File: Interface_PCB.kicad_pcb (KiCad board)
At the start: 2 copper layers, 46.5 x 47.9 mm, 46 parts, among them IC1 STM32L412RBT6P, U1 AMS1117-3.3, Y1 Crystal, Y2 Crystal

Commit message: Added BOM, position and gerber files
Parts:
- LMS1: footprint Capacitor_SMD:C_0603_1608Metric -> Inductor_SMD:L_0603_1608Metric
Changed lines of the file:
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@@
       (drillshape 0)
       (scaleselection 1)
-      (outputdirectory "drill files/")
+      (outputdirectory "drill files/gerber/")
     )
   )
@@
     )
     (fp_line (start -4.65 -4.65) (end 4.65 -4.65) (layer "F.SilkS") (width 0.2))
-    (fp_line (start -4.65 4.65) (end -4.65 -4.65) (layer "F.SilkS") (width 0.2))
     (fp_line (start 4.65 4.65) (end -4.65 4.65) (layer "F.SilkS") (width 0.2))
+    (fp_line (start -4.65 4.65) (end -4.65 -4.65) (layer "F.SilkS") (width 0.2))
     (fp_line (start 4.65 -4.65) (end 4.65 4.65) (layer "F.SilkS") (width 0.2))
     (fp_circle (center -6.225 -4.5) (end -6.225 -4.375) (layer "F.SilkS") (width 0.25) (fill none))
-    (fp_line (start -6.725 -6.725) (end 6.725 -6.725) (layer "F.CrtYd") (width 0.05))
     (fp_line (start 6.725 -6.725) (end 6.725 6.725) (layer "F.CrtYd") (width 0.05))
-    (fp_line (start -6.725 6.725) (end -6.725 -6.725) (layer "F.CrtYd") (width 0.05))
     (fp_line (start 6.725 6.725) (end -6.725 6.725) (layer "F.CrtYd") (width 0.05))
+    (fp_line (start -6.725 -6.725) (end 6.725 -6.725) (layer "F.CrtYd") (width 0.05))
+    (fp_line (start -6.725 6.725) (end -6.725 -6.725) (layer "F.CrtYd") (width 0.05))
+    (fp_line (start -5 -4.5) (end -4.5 -5) (layer "F.Fab") (width 0.1))
+    (fp_line (start 5 -5) (end 5 5) (layer "F.Fab") (width 0.1))
     (fp_line (start -5 5) (end -5 -5) (layer "F.Fab") (width 0.1))
     (fp_line (start -5 -5) (end 5 -5) (layer "F.Fab") (width 0.1))
     (fp_line (start 5 5) (end -5 5) (layer "F.Fab") (width 0.1))
-    (fp_line (start 5 -5) (end 5 5) (layer "F.Fab") (width 0.1))
-    (fp_line (start -5 -4.5) (end -4.5 -5) (layer "F.Fab") (width 0.1))
     (pad "1" smd rect locked (at -5.738 -3.75 90) (size 0.3 1.475) (layers "F.Cu" "F.Paste" "F.Mask")
       (net 3 "+3V3") (pinfunction "VBAT") (pintype "passive"))
@@
     (pad "" np_thru_hole circle (at 0 0) (size 2.1 2.1) (drill 2.1) (layers *.Cu *.Mask))
   )
-  (footprint "Capacitor_SMD:C_0603_1608Metric" (layer "F.Cu")
+  (footprint "Inductor_SMD:L_0603_1608Metric" (layer "F.Cu")
     (at 127.0508 111.506)
-    (descr "Capacitor SMD 0603 (1608 Metric), square (rectangular) end terminal, IPC_7351 nominal, (Body size source: IPC-SM-782 page 76, https://www.pcb-3d.com/wordpress/wp-content/uploads/ipc-sm-782a_amendment_1_and_2.pdf), generated with kicad-footprint-generator")
-    (tags "capacitor")
+    (descr "Inductor SMD 0603 (1608 Metric), square (rectangular) end terminal, IPC_7351 nominal, (Body size source: http://www.tortai-tech.com/upload/download/2011102023233369053.pdf), generated with kicad-footprint-generator")
+    (tags "inductor")
     (property "Sheetfile" "Interface_PCB.kicad_sch")
     (property "Sheetname" "")
     (attr smd)
-    (fp_text reference "LMS1" (at -2.54 -0.0254 180) (layer "F.SilkS")
-      (effects (font (size 0.5 0.5) (thickness 0.125)))
+    (fp_text reference "LMS1" (at -3.302 0.0254) (layer "F.SilkS")
+      (effects (font (size 1 1) (thickness 0.15)))
     )
     (fp_text value "39nH" (at 0 1.43) (layer "F.Fab")
@@
       (effects (font (size 0.4 0.4) (thickness 0.06)))
     )
-    (fp_line (start -0.14058 -0.51) (end 0.14058 -0.51) (layer "F.SilkS") (width 0.12))
-    (fp_line (start -0.14058 0.51) (end 0.14058 0.51) (layer "F.SilkS") (width 0.12))
+    (fp_line (start -0.162779 -0.51) (end 0.162779 -0.51) (layer "F.SilkS") (width 0.12))
+    (fp_line (start -0.162779 0.51) (end 0.162779 0.51) (layer "F.SilkS") (width 0.12))
     (fp_line (start -1.48 -0.73) (end 1.48 -0.73) (layer "F.CrtYd") (width 0.05))
-    (fp_line (start 1.48 -0.73) (end 1.48 0.73) (layer "F.CrtYd") (width 0.05))
     (fp_line (start -1.48 0.73) (end -1.48 -0.73) (layer "F.CrtYd") (width 0.05))
+    (fp_line (start 1.48 -0.73) (end 1.48 0.73) (layer "F.CrtYd") (width 0.05))
     (fp_line (start 1.48 0.73) (end -1.48 0.73) (layer "F.CrtYd") (width 0.05))
-    (fp_line (start -0.8 0.4) (end -0.8 -0.4) (layer "F.Fab") (width 0.1))
+    (fp_line (start 0.8 -0.4) (end 0.8 0.4) (layer "F.Fab") (width 0.1))
     (fp_line (start -0.8 -0.4) (end 0.8 -0.4) (layer "F.Fab") (width 0.1))
+    (fp_line (start -0.8 0.4) (end -0.8 -0.4) (layer "F.Fab") (width 0.1))
     (fp_line (start 0.8 0.4) (end -0.8 0.4) (layer "F.Fab") (width 0.1))
-    (fp_line (start 0.8 -0.4) (end 0.8 0.4) (layer "F.Fab") (width 0.1))
-    (pad "1" smd roundrect (at -0.775 0) (size 0.9 0.95) (layers "F.Cu" "F.Paste" "F.Mask") (roundrect_rratio 0.25)
+    (pad "1" smd roundrect (at -0.7875 0) (size 0.875 0.95) (layers "F.Cu" "F.Paste" "F.Mask") (roundrect_rratio 0.25)
       (net 3 "+3V3") (pinfunction "1") (pintype "passive"))
-    (pad "2" smd roundrect (at 0.775 0) (size 0.9 0.95) (layers "F.Cu" "F.Paste" "F.Mask") (roundrect_rratio 0.25)
+    (pad "2" smd roundrect (at 0.7875 0) (size 0.875 0.95) (layers "F.Cu" "F.Paste" "F.Mask") (roundrect_rratio 0.25)
       (net 4 "+3.3VA") (pinfunction "2") (pintype "passive"))
-    (model "${KICAD6_3DMODEL_DIR}/Capacitor_SMD.3dshapes/C_0603_1608Metric.wrl"
+    (model "${KICAD6_3DMODEL_DIR}/Inductor_SMD.3dshapes/L_0603_1608Metric.wrl"
       (offset (xyz 0 0 0))
       (scale (xyz 1 1 1))

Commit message: Added TVS diode and External Voltage (BOM and gerber included)
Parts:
- added DEXT1: D_Schottky, SamacSys_Parts:AQ120501ETG, F.Cu at (153.5, 111.5)
- added VEXT: Conn_01x02_Male, Connector_PinHeader_2.54mm:PinHeader_1x02_P2.54mm_Vertical, F.Cu at (157.2, 111.8)
- LMS1: footprint Inductor_SMD:L_0603_1608Metric -> Inductor_SMD:L_0805_2012Metric
- LR1: footprint Inductor_SMD:L_0402_1005Metric -> Inductor_SMD:L_0805_2012Metric
- moved CR3 0.18 mm to (150.1, 112.5)
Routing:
- net Net-(J9-Pad1): track 0.00 -> 3.41 mm
- net I2C1_SCL: track 39.8 -> 43.0 mm
- net I2C1_SDA: track 40.1 -> 43.0 mm
- net /VEXT: track 1.30 -> 3.99 mm
- net GND: track 87.4 -> 89.7 mm, vias 20 -> 21

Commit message: Corrected the annotations
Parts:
- renumbered I2C1 to J1, USART1 to J2, I2C2 to J3, USART2 to J4, JTAG to J5, SPI to J6, USB to J7, VEXT to J9
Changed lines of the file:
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@@
   (net 68 "Net-(CR1-Pad1)")
   (net 69 "Net-(LR1-Pad1)")
-  (net 70 "Net-(J9-Pad1)")
+  (net 70 "Net-(DEXT1-Pad2)")
   (footprint "SamacSys_Parts:502382-0470" (layer "F.Cu")
     (at 119.2954 115.5436 90)
@@
     (property "Sheetname" "")
     (attr smd)
-    (fp_text reference "I2C2" (at -3.557 2.5948 180) (layer "F.SilkS")
+    (fp_text reference "J3" (at -3.5316 1.7102 180) (layer "F.SilkS")
       (effects (font (size 1.27 1.27) (thickness 0.254)))
     )
@@
     )
     (fp_line (start -4.65 -4.65) (end 4.65 -4.65) (layer "F.SilkS") (width 0.2))
-    (fp_line (start 4.65 -4.65) (end 4.65 4.65) (layer "F.SilkS") (width 0.2))
-    (fp_line (start 4.65 4.65) (end -4.65 4.65) (layer "F.SilkS") (width 0.2))
     (fp_line (start -4.65 4.65) (end -4.65 -4.65) (layer "F.SilkS") (width 0.2))
+    (fp_line (start 4.65 4.65) (end -4.65 4.65) (layer "F.SilkS") (width 0.2))
+    (fp_line (start 4.65 -4.65) (end 4.65 4.65) (layer "F.SilkS") (width 0.2))
     (fp_circle (center -6.225 -4.5) (end -6.225 -4.375) (layer "F.SilkS") (width 0.25) (fill none))
+    (fp_line (start 6.725 -6.725) (end 6.725 6.725) (layer "F.CrtYd") (width 0.05))
     (fp_line (start 6.725 6.725) (end -6.725 6.725) (layer "F.CrtYd") (width 0.05))
     (fp_line (start -6.725 -6.725) (end 6.725 -6.725) (layer "F.CrtYd") (width 0.05))
-    (fp_line (start 6.725 -6.725) (end 6.725 6.725) (layer "F.CrtYd") (width 0.05))
     (fp_line (start -6.725 6.725) (end -6.725 -6.725) (layer "F.CrtYd") (width 0.05))
-    (fp_line (start 5 5) (end -5 5) (layer "F.Fab") (width 0.1))
     (fp_line (start -5 5) (end -5 -5) (layer "F.Fab") (width 0.1))
-    (fp_line (start 5 -5) (end 5 5) (layer "F.Fab") (width 0.1))
+    (fp_line (start 5 5) (end -5 5) (layer "F.Fab") (width 0.1))
     (fp_line (start -5 -4.5) (end -4.5 -5) (layer "F.Fab") (width 0.1))
+    (fp_line (start 5 -5) (end 5 5) (layer "F.Fab") (width 0.1))
     (fp_line (start -5 -5) (end 5 -5) (layer "F.Fab") (width 0.1))
     (pad "1" smd rect locked (at -5.738 -3.75 90) (size 0.3 1.475) (layers "F.Cu" "F.Paste" "F.Mask")
@@
     (property "Sheetname" "")
     (attr smd)
-    (fp_text reference "SPI" (at 10.1478 -6.3186) (layer "F.SilkS")
+    (fp_text reference "J6" (at 10.1478 -6.3186) (layer "F.SilkS")
       (effects (font (size 1.27 1.27) (thickness 0.254)))
     )
@@
       (net 1 "/VEXT") (pinfunction "K") (pintype "passive"))
     (pad "2" smd rect locked (at 0.325 0) (size 0.35 0.6) (layers "F.Cu" "F.Paste" "F.Mask")
-      (net 70 "Net-(J9-Pad1)") (pinfunction "A") (pintype "passive"))
+      (net 70 "Net-(DEXT1-Pad2)") (pinfunction "A") (pintype "passive"))
     (model "D:\\PCB DES KICAD\\SamacSys_Parts.3dshapes\\AQ1205-01ETG.stp"
       (offset (xyz 0 0 0))
@@
     (property "Sheetname" "")
     (attr smd)
-    (fp_text reference "USART2" (at 5.3068 -1.27 180) (layer "F.SilkS")
+    (fp_text reference "J4" (at 5.3068 -1.27 180) (layer "F.SilkS")
       (effects (font (size 1.27 1.27) (thickness 0.254)))
     )
@@
     (property "Sheetname" "")
     (attr smd)
-    (fp_text reference "I2C1" (at 0.2798 2.2284) (layer "F.SilkS")
+    (fp_text reference "J1" (at 2.8706 1.6696) (layer "F.SilkS")
       (effects (font (size 1.27 1.27) (thickness 0.254)))
     )
@@
     (property "Sheetname" "")
     (attr smd)
-    (fp_text reference "USART1" (at -7.747 -2.5316) (layer "F.SilkS")
+    (fp_text reference "J2" (at -5.7404 -2.6586) (layer "F.SilkS")
       (effects (font (size 1.27 1.27) (thickness 0.254)))
     )
@@
     (property "Sheetname" "")
     (attr smd)
-    (fp_text reference "JTAG" (at 4.4704 0.3991 180) (layer "F.SilkS")
+    (fp_text reference "J5" (at 3.8862 4.4377 180) (layer "F.SilkS")
       (effects (font (size 1.27 1.27) (thickness 0.254)))
     )
@@
     (property "Sheetname" "")
     (attr through_hole)
-    (fp_text reference "USB" (at 5.8674 1.397 180) (layer "F.SilkS")
+    (fp_text reference "J7" (at 5.8674 1.397 180) (layer "F.SilkS")
       (effects (font (size 1.27 1.27) (thickness 0.254)))
     )
@@
     (property "Sheetname" "")
     (attr through_hole)
-    (fp_text reference "VEXT" (at 0 -2.3572) (layer "F.SilkS")
+    (fp_text reference "J9" (at 0 -2.3572) (layer "F.SilkS")
       (effects (font (size 1 1) (thickness 0.15)))
     )
@@
     (fp_line (start -1.27 -0.635) (end -0.635 -1.27) (layer "F.Fab") (width 0.1))
     (pad "1" thru_hole rect (at 0 0) (size 1.7 1.7) (drill 1) (layers *.Cu *.Mask)
-      (net 70 "Net-(J9-Pad1)") (pinfunction "Pin_1") (pintype "passive"))
+      (net 70 "Net-(DEXT1-Pad2)") (pinfunction "Pin_1") (pintype "passive"))
     (pad "2" thru_hole oval (at 0 2.54) (size 1.7 1.7) (drill 1) (layers *.Cu *.Mask)
       (net 2 "GND") (pinfunction "Pin_2") (pintype "passive"))

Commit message: Added Full BOM and gerber
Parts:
- removed J9: Conn_01x02_Male, Connector_PinHeader_2.54mm:PinHeader_1x02_P2.54mm_Vertical
- added J8: Conn_01x02_Male, Connector_PinHeader_2.54mm:PinHeader_1x02_P2.54mm_Vertical, F.Cu at (157.2, 111.8)

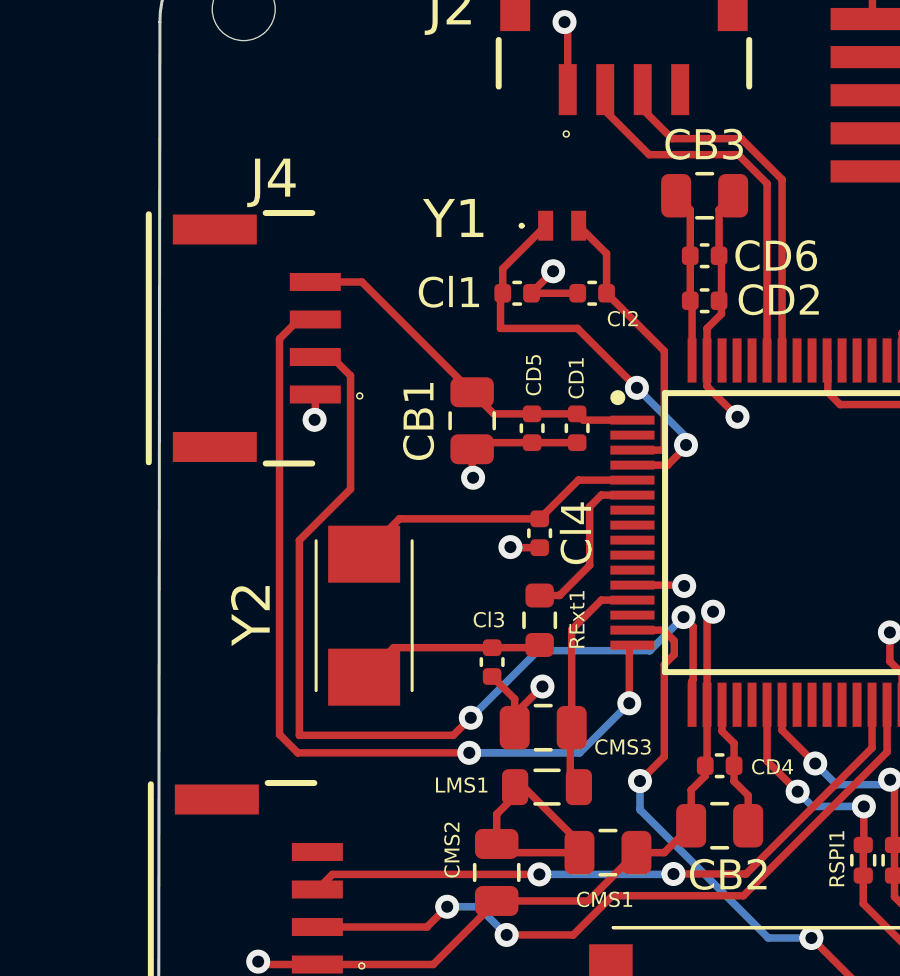
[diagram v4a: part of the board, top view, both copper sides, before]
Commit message: Oscillators are brought closer
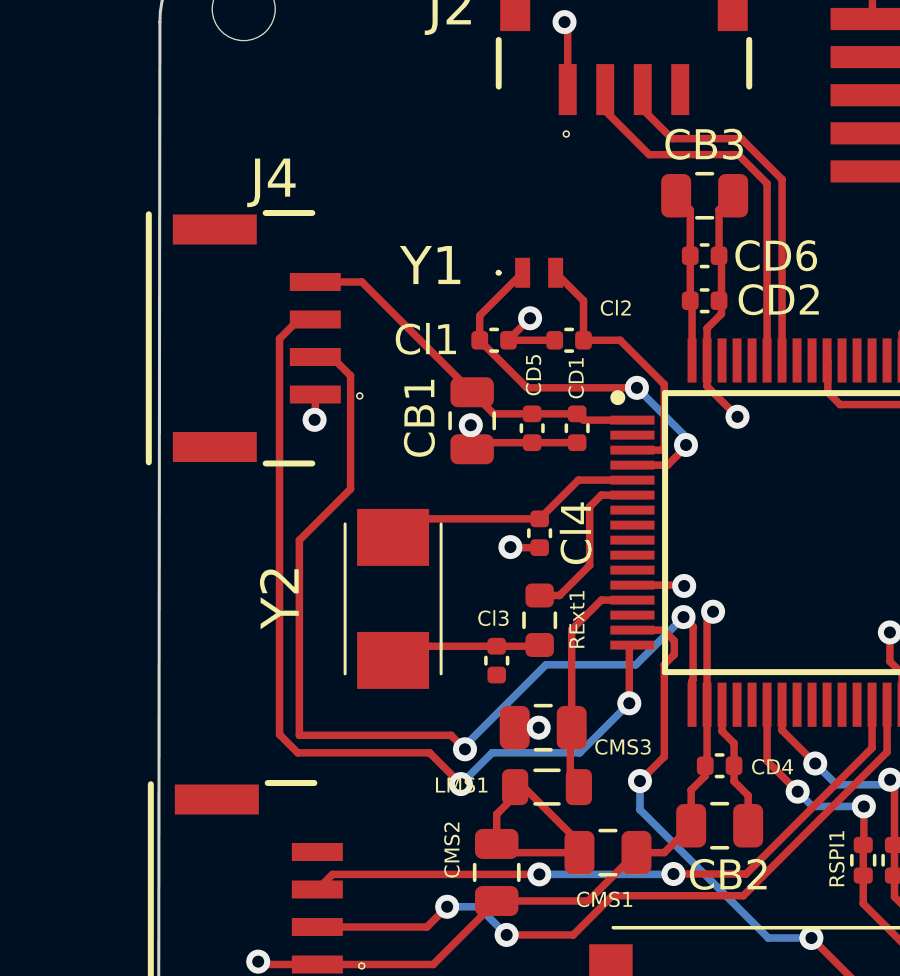
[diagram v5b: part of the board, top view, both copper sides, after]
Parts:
- moved Cl1 1.75 mm to (125.3, 96.6)
- moved Cl2 1.75 mm to (127.8, 96.6)
- moved Y1 1.75 mm to (126.8, 94.4)
- moved Y2 1.12 mm to (121.9, 105.2)
- moved Cl3 0.16 mm to (125.4, 107.3)
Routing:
- net GND: track 89.7 -> 86.6 mm
- net HSE_IN: track 9.97 -> 8.77 mm
- net Net-(Cl3-Pad1): track 6.30 -> 5.22 mm
- net USART2_TX: track 29.2 -> 30.1 mm
- net LSE_OUT: track 14.1 -> 13.5 mm
- net LSE_IN: track 9.71 -> 9.17 mm
